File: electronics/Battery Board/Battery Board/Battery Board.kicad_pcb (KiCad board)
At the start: 2 copper layers, 92 x 88 mm, 20 parts, among them Q1 IRF7404, Q2 IRF7404, U1 MAX1924XEEE+

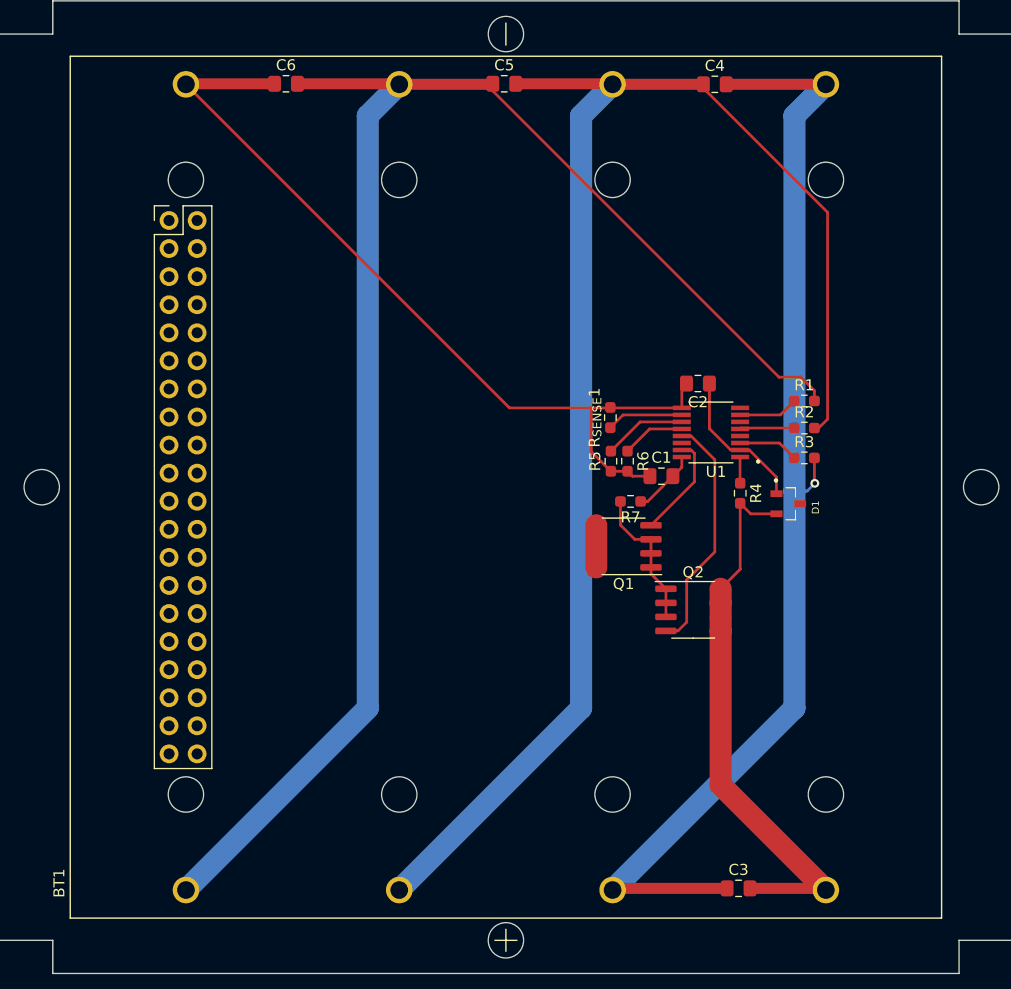
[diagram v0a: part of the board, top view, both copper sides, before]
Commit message: Battery protection circuit added
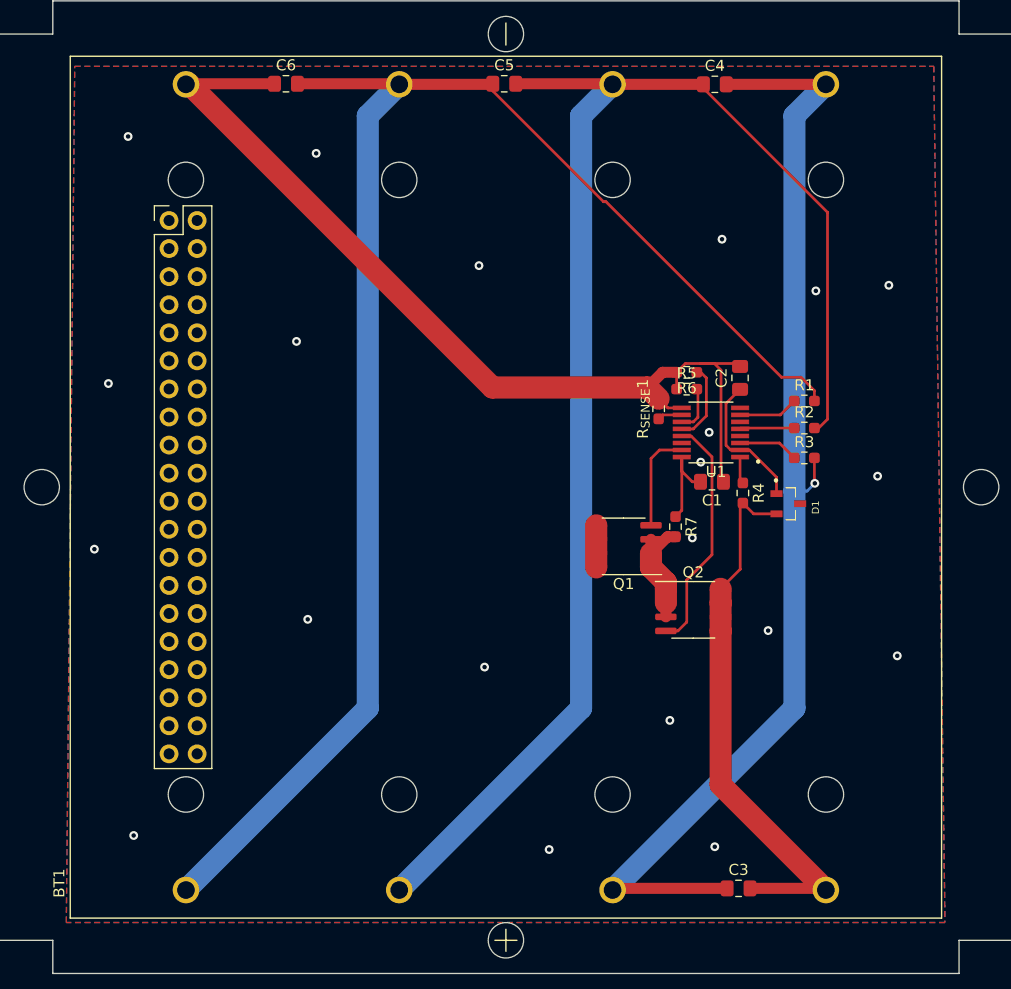
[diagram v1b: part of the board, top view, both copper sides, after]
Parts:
- moved R6 9.67 mm to (254.5, 35.3), turned to 180 degrees
- moved R5 9.46 mm to (254.5, 36.8), turned to 0 degrees
- moved R7 4.66 mm to (253.5, 49.3), turned to -90 degrees
- moved C1 4.60 mm to (256.8, 45.2), turned to 180 degrees
- moved R_{SENSE}1 4.44 mm to (252.0, 38.6)
- moved C2 3.84 mm to (259.3, 35.8), turned to 90 degrees
- moved R4 0.24 mm to (259.6, 46.2)
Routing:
- net GNDPWR: track 77.6 -> 91.2 mm
- net GND: track 6.94 -> 2.25 mm, vias 0 -> 20
- net Net-(R5-Pad2): track 7.51 -> 4.22 mm
- net Net-(C1-Pad2): track 5.93 -> 8.73 mm
- net Net-(Q1-Pad1): track 13.0 -> 10.4 mm
- net Net-(R6-Pad1): track 5.75 -> 7.22 mm
- net Net-(C2-Pad1): track 13.5 -> 12.8 mm
- net (no net): vias 0 -> 1
- added copper zone on B.Cu, net GND
- added copper zone on F.Cu, net GND

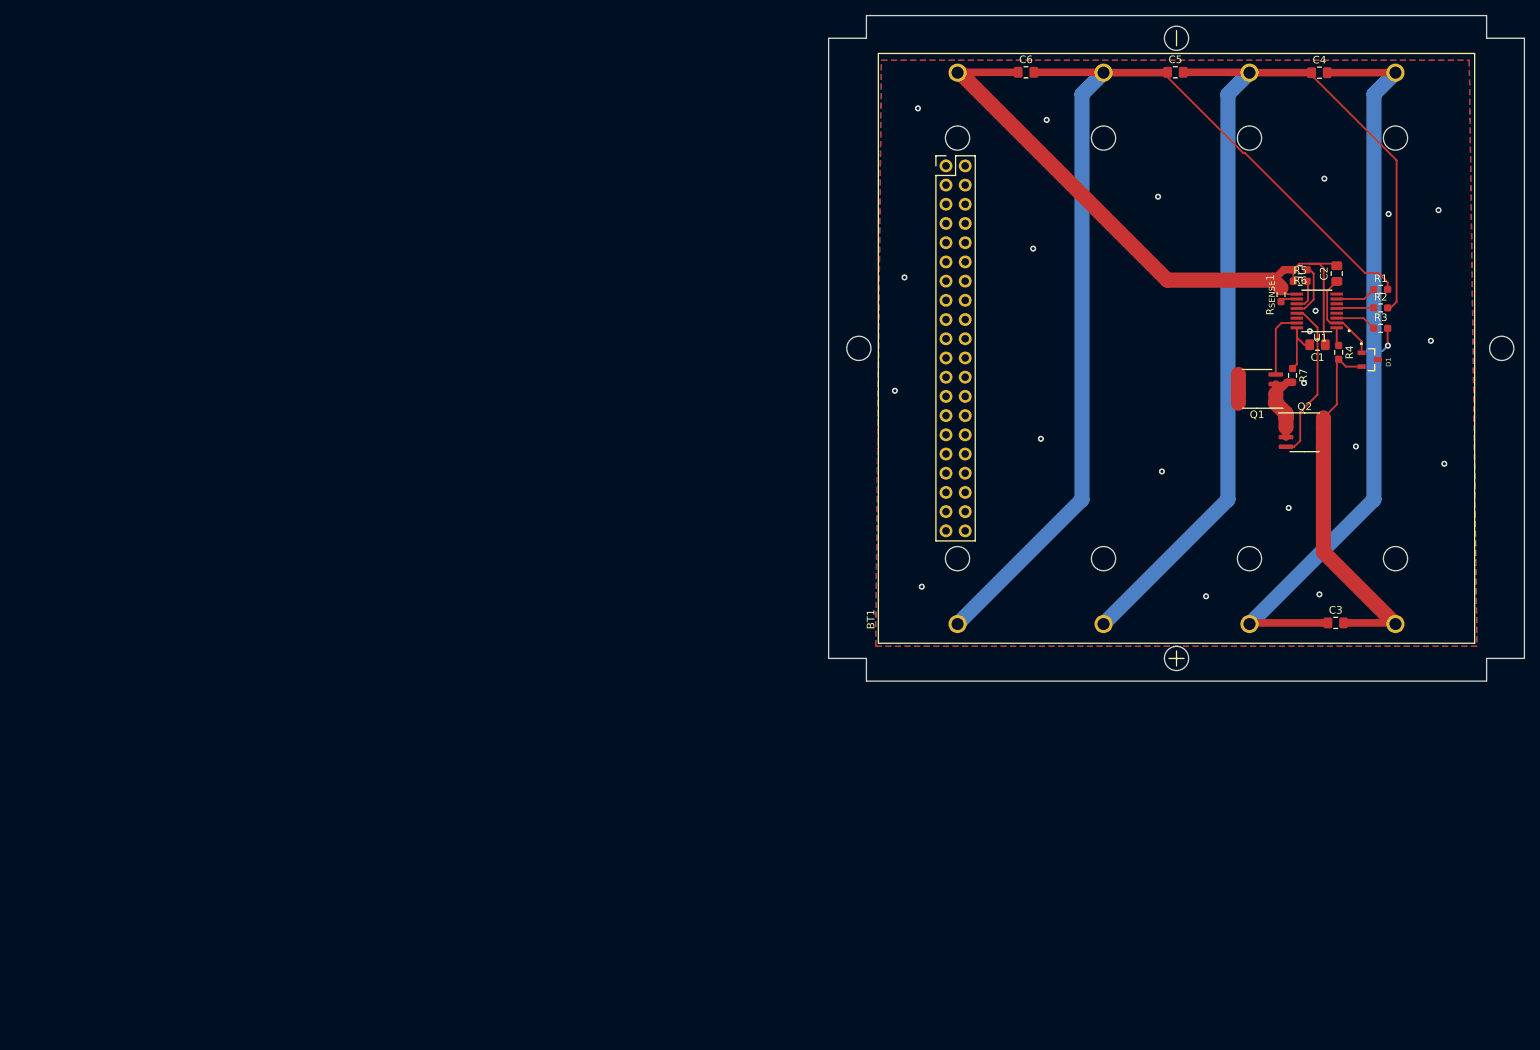
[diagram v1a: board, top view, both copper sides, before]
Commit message: Batter Board almost finished
TODO
- Change mosfets&shunt resistor to new choice
- Adjust inductor for higher voltage
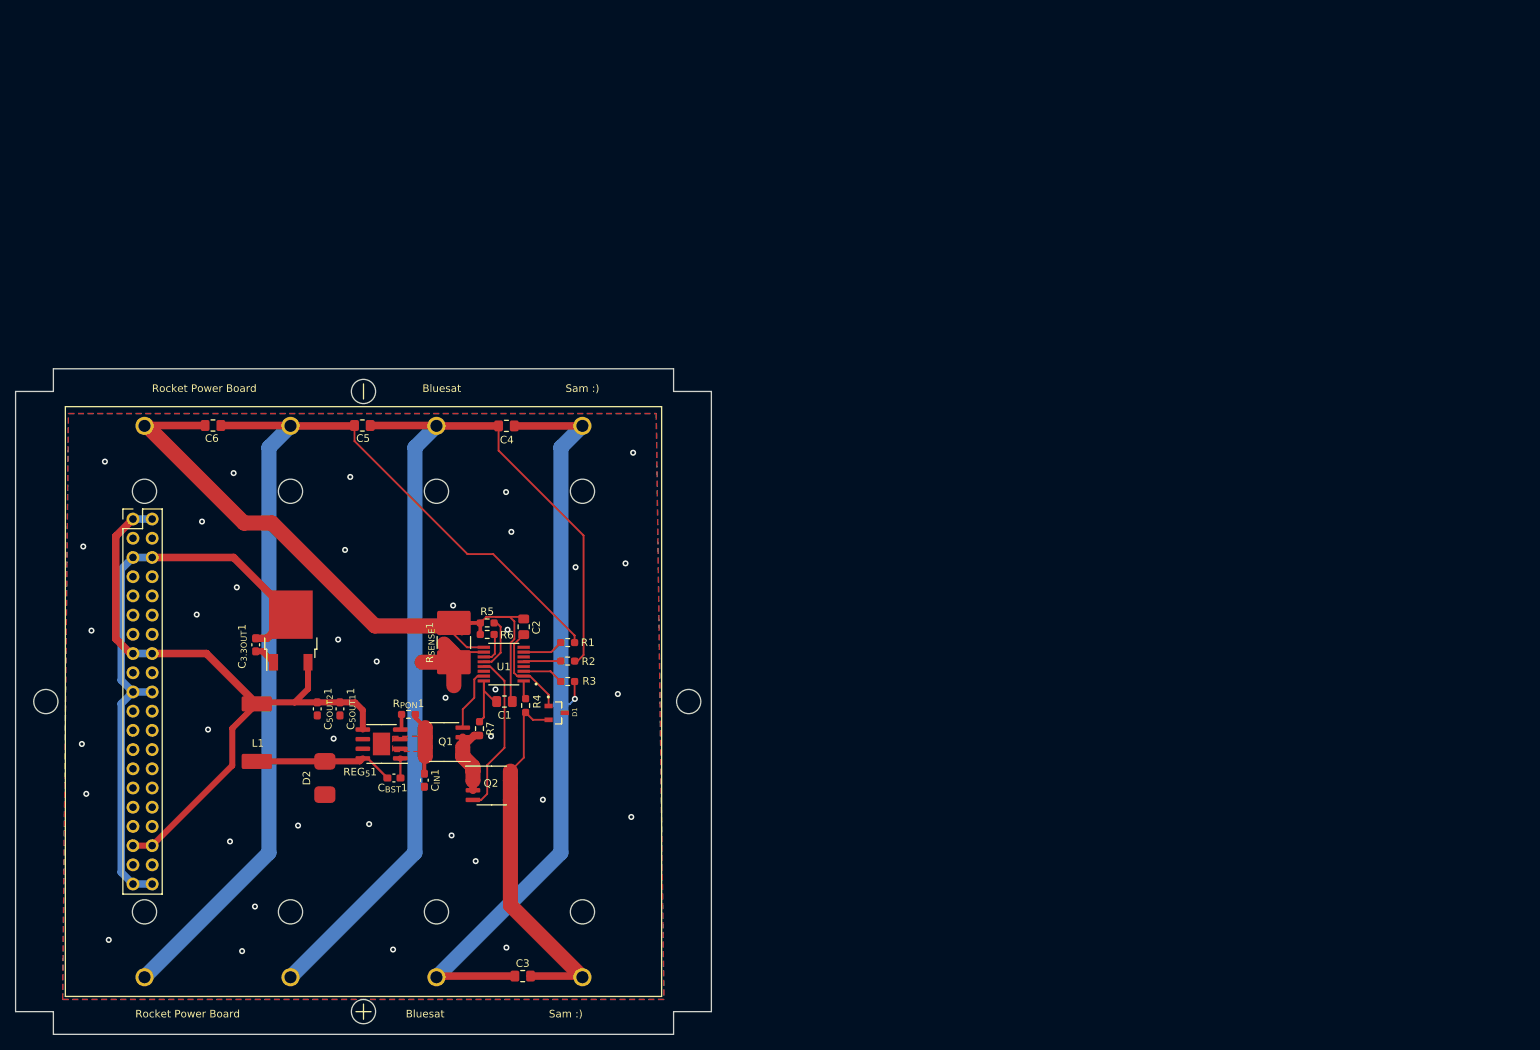
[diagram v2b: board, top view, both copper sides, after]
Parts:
- added C_{3.3OUT}1: 22uF, Capacitor_SMD:C_0603_1608Metric_Pad1.08x0.95mm_HandSolder, F.Cu at (116.4, 84.9)
- added C_{5OUT1}1: 22uF, Capacitor_SMD:C_0603_1608Metric_Pad1.08x0.95mm_HandSolder, F.Cu at (127.5, 93.4)
- added C_{5OUT2}1: 22uF, Capacitor_SMD:C_0603_1608Metric_Pad1.08x0.95mm_HandSolder, F.Cu at (124.5, 93.4)
- added C_{BST}1: 0.1uF, Capacitor_SMD:C_0603_1608Metric_Pad1.08x0.95mm_HandSolder, F.Cu at (134.7, 102.5)
- added C_{IN}1: 10uF, Capacitor_SMD:C_0603_1608Metric_Pad1.08x0.95mm_HandSolder, F.Cu at (138.7, 102.8)
- added D2: SSB43L, Custom footprints:SSB43L hand solder, F.Cu at (125.5, 102.5)
- added L1: 3.8uF, Custom footprints:CDRH104R inductor, F.Cu at (116.5, 96.5)
- added REG_{5}1: ADP2302ARDZ-5.0, Package_SO:SOIC-8-1EP_3.9x4.9mm_P1.27mm_EP2.29x3mm, F.Cu at (133.0, 98.0)
- added R_{PON}1: 100K, Resistor_SMD:R_0603_1608Metric_Pad0.98x0.95mm_HandSolder, F.Cu at (136.6, 94.1)
- added Reg_{3.3}1: AZ1117-3.3, Package_TO_SOT_SMD:TO-252-2, F.Cu at (121.0, 83.0)
- R_{SENSE}1: footprint Resistor_SMD:R_0603_1608Metric_Pad0.98x0.95mm_HandSolder -> Resistor_SMD:R_2816_7142Metric_Pad3.20x4.45mm_HandSolder
- moved R_{SENSE}1 118.6 mm to (142.6, 84.6)
- moved C1 117.4 mm to (149.3, 92.4)
- moved R4 117.2 mm to (152.1, 92.9)
- moved BT1 117.2 mm to (130.7, 92.4)
- moved C2 117.2 mm to (151.8, 82.5)
- moved C4 117.2 mm to (149.6, 56.0)
- moved C5 117.2 mm to (130.5, 55.9)
- moved C6 117.2 mm to (110.8, 55.9)
- moved D1 117.2 mm to (156.2, 93.9)
- moved Q1 117.2 mm to (141.3, 97.8)
- moved Q2 117.2 mm to (147.6, 103.5)
- moved R5 117.2 mm to (147.0, 83.5)
- moved R6 117.2 mm to (147.0, 82.0)
- moved R7 117.2 mm to (146.0, 96.0)
- moved R8 117.2 mm to (130.7, 92.4)
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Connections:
- net Net-(R8-Pad1) renamed +5V
- net Net-(R8-Pad10) renamed +3V3
- R8 pad 11: Net-(R8-Pad11) -> GND
- R8 pad 14: Net-(R8-Pad11) -> GND
- R8 pad 17: Net-(R8-Pad11) -> GND
- R8 pad 19: Net-(R8-Pad11) -> GND
- R8 pad 2: Net-(R8-Pad11) -> GND
- R8 pad 22: Net-(R8-Pad11) -> GND
- R8 pad 24: Net-(R8-Pad11) -> GND
- R8 pad 27: Net-(R8-Pad11) -> GND
- R8 pad 30: Net-(R8-Pad11) -> GND
- R8 pad 32: Net-(R8-Pad11) -> GND
- R8 pad 34: Net-(R8-Pad11) -> GND
- R8 pad 37: Net-(R8-Pad11) -> GND
- R8 pad 39: Net-(R8-Pad11) -> GND
- R8 pad 4: Net-(R8-Pad11) -> GND
- R8 pad 7: Net-(R8-Pad11) -> GND
- R8 pad 9: Net-(R8-Pad11) -> GND
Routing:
- net +5V: track 0.00 -> 91.7 mm
- net +3V3: track 0.00 -> 80.8 mm
- net Net-(C_{BST}1-Pad1): track 0.00 -> 18.5 mm
- net GND: track 2.25 -> 17.7 mm, vias 20 -> 37
- net VPP: track 3.81 -> 8.43 mm
- net GNDPWR: track 91.2 -> 95.6 mm
- net Net-(C_{BST}1-Pad2): track 0.00 -> 2.61 mm
- net Net-(REG_{5}1-Pad4): track 0.00 -> 2.08 mm
- net Net-(BT1-Pad1+): track 140.5 -> 141.4 mm
- net Net-(Q1-Pad4): track 9.15 -> 8.46 mm
- added copper zone on F.Cu, net VPP
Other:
- board text added: "Bluesat"
- board text added: "Rocket Power Board"
- board text added: "Sam :)"

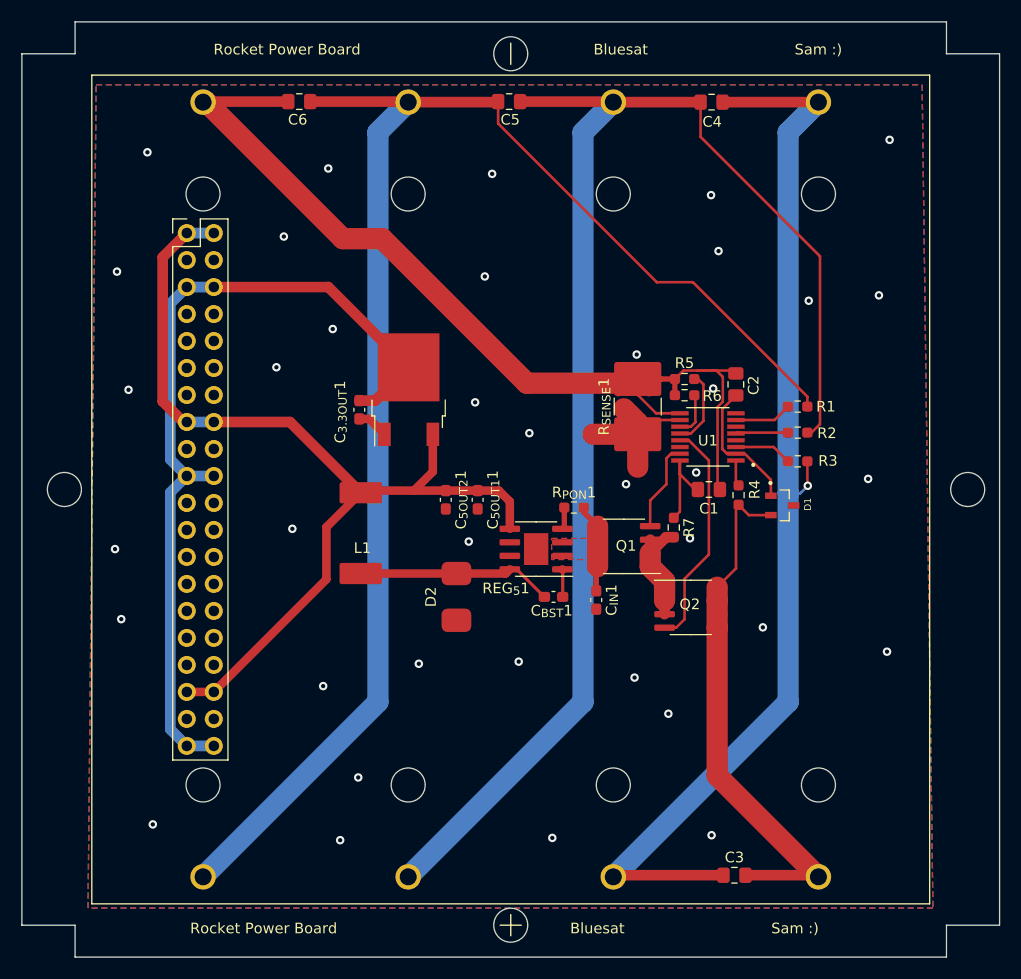
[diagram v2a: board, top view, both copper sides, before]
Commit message: Finalised PCB, working schematic
Sending to Fab tomorrow, schematic could do with a little cleanup.
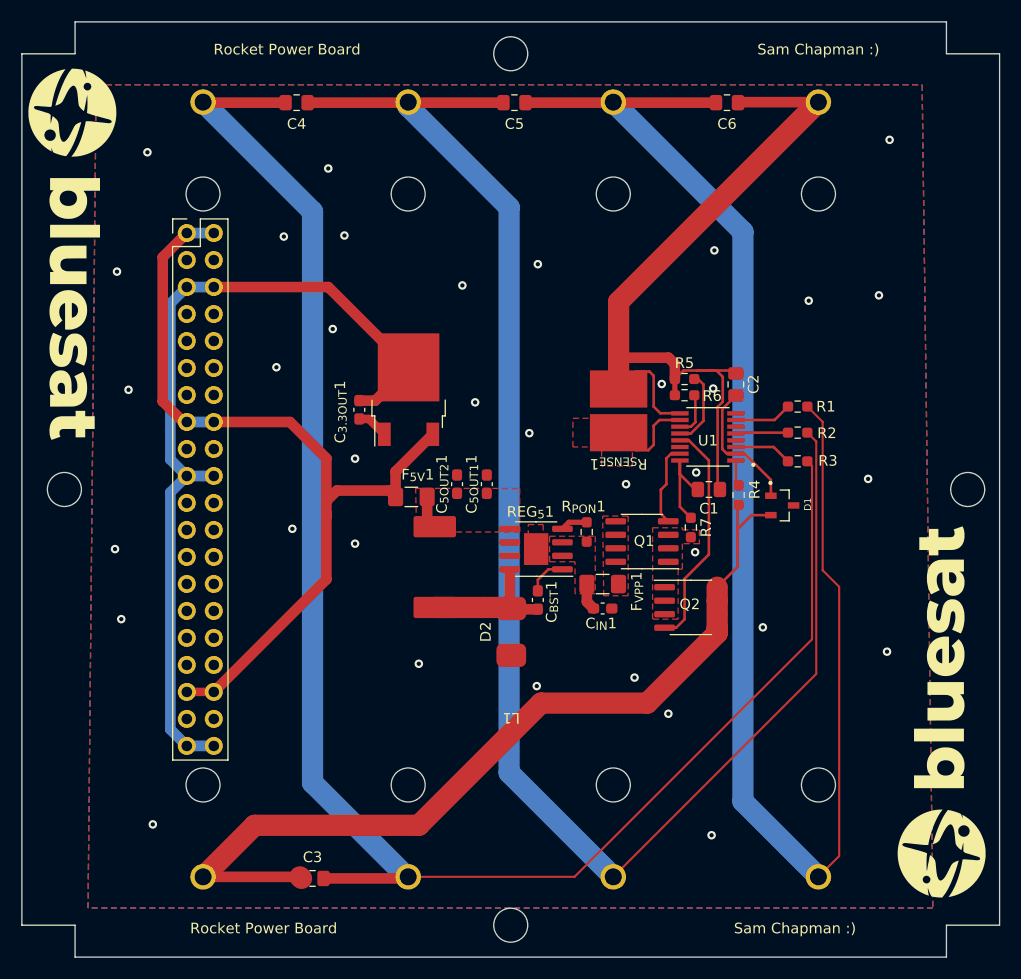
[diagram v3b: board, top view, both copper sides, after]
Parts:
- added F_{5V}1: 2A, Fuse:Fuse_1206_3216Metric_Pad1.42x1.75mm_HandSolder, F.Cu at (121.3, 93.1)
- added F_{VPP}1: 3A, Fuse:Fuse_1206_3216Metric_Pad1.42x1.75mm_HandSolder, F.Cu at (139.3, 101.3)
- added G***: LOGO, Bluesat:Logo, F.Cu at (89.4, 70.3)
- added G***: LOGO, Bluesat:Logo, F.Cu at (171.2, 113.3)
- BT1: moved to B.Cu
- L1: value 3.8uF -> 10uF
- Q1, Q2: value IRF7404 -> AOSP21321
- R_{SENSE}1: value 0.02 -> 0.047; footprint Resistor_SMD:R_2816_7142Metric_Pad3.20x4.45mm_HandSolder -> Bluesat:WSHP2818 Shunt resistor Vishay
- moved C6 40.3 mm to (151.0, 56.0), turned to 180 degrees
- moved C3 39.7 mm to (112.0, 129.0), turned to 180 degrees
- moved C4 39.1 mm to (110.5, 56.0), turned to 180 degrees
- moved L1 7.66 mm to (123.5, 99.7)
- moved D2 6.12 mm to (130.7, 105.8)
- moved R_{PON}1 2.59 mm to (137.8, 96.4), turned to -90 degrees
- moved R_{SENSE}1 1.84 mm to (140.8, 85.0), turned to 180 degrees
- moved C_{5OUT2}1 1.81 mm to (125.6, 91.9), turned to 90 degrees
- moved Q1 1.76 mm to (143.0, 97.3)
- moved C_{5OUT1}1 1.70 mm to (128.4, 91.9), turned to 90 degrees
- moved R7 1.61 mm to (147.6, 96.0)
- moved C_{BST}1 1.50 mm to (133.2, 102.8), turned to 90 degrees
- moved C_{IN}1 1.00 mm to (139.3, 103.6), turned to 0 degrees
- moved C5 0.51 mm to (131.0, 56.0), turned to 180 degrees
- turned C2 to -90 degrees
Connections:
- C2 pad 1: Net-(C2-Pad1) -> GNDPWR
- C2 pad 2: GNDPWR -> Net-(D1-Pad1)
- C_{5OUT1}1 pad 1: +5V -> Net-(C_{5OUT1}1-Pad1)
- C_{5OUT2}1 pad 1: +5V -> Net-(C_{5OUT1}1-Pad1)
- D1 pad 1: Net-(C2-Pad1) -> Net-(D1-Pad1)
- L1 pad 2: +5V -> Net-(C_{5OUT1}1-Pad1)
- Q1 pad 5: VPP -> Net-(Q1-Pad5)
- Q1 pad 6: VPP -> Net-(Q1-Pad5)
- Q1 pad 7: VPP -> Net-(Q1-Pad5)
- Q1 pad 8: VPP -> Net-(Q1-Pad5)
- REG_{5}1 pad 5: +5V -> Net-(C_{5OUT1}1-Pad1)
- U1 pad 2: Net-(C2-Pad1) -> Net-(D1-Pad1)
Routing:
- net Net-(BT1-Pad3+): track 104.8 -> 161.0 mm, vias 1 -> 0
- net Net-(BT1-Pad4+): track 61.1 -> 86.2 mm
- net Net-(BT1-Pad2+): track 134.4 -> 149.7 mm
- net GNDPWR: track 95.6 -> 80.3 mm
- net Net-(D1-Pad1): track 0.00 -> 12.8 mm
- net Net-(C2-Pad1): track 12.8 -> 0.00 mm
- net +5V: track 91.7 -> 80.4 mm
- net Net-(Q1-Pad1): track 10.4 -> 0.00 mm
- net GND: track 17.7 -> 11.6 mm, vias 37 -> 35
- net VPP: track 8.43 -> 2.56 mm
- net Net-(C_{BST}1-Pad1): track 18.5 -> 13.9 mm
- net Net-(BT1-Pad1+): track 141.4 -> 145.4 mm
- net Net-(C_{5OUT1}1-Pad1): track 0.00 -> 3.10 mm
- net Net-(C_{BST}1-Pad2): track 2.61 -> 3.76 mm
- net Net-(Q1-Pad4): track 8.46 -> 7.88 mm
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- added copper zone on F.Cu, net Net-(C_{5OUT1}1-Pad1)
- added copper zone on F.Cu, net Net-(Q1-Pad1)
- added copper zone on F.Cu, net Net-(Q1-Pad5)
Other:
- board text added: "Sam Chapman :)"
- board text removed: "Bluesat"
- board text removed: "Sam :)"
